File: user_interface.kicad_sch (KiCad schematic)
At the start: 33 parts, among them CN5 Line out, CN6 Headphone, J2 SWD, J3 I2C, J6 SPI, J9 Serial, P1 GPIO, SW4 BTN1, SW5 BTN2

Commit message: Start routing through the new signal layer.
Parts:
- removed R32: Zero, Resistor_SMD:R_2010_5025Metric, symbol Device:R_Small
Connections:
- net HPJ_R is gone; now on net HEADPHONE_R: CN6.3
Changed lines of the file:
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@@
 	(wire
 		(pts
-			(xy 212.09 53.34) (xy 220.98 53.34)
+			(xy 212.09 53.34) (xy 232.41 53.34)
 		)
 		(stroke
@@
 	(wire
 		(pts
-			(xy 226.06 53.34) (xy 232.41 53.34)
-		)
-		(stroke
-			(width 0)
-			(type default)
-		)
-	)
-	(wire
-		(pts
 			(xy 68.58 175.26) (xy 74.93 175.26)
 		)
@@
 		)
 	)
-	(label "HPJ_R"
-		(at 226.06 53.34 0)
-		(fields_autoplaced yes)
-		(effects
-			(font
-				(size 1.27 1.27)
-			)
-			(justify left bottom)
-		)
-	)
 	(label "BTN2_CR"
 		(at 171.45 48.26 0)
@@
 					(unit 1)
 				)
-			)
-		)
-	)
-	(symbol
-		(lib_id "Device:R_Small")
-		(at 223.52 53.34 90)
-		(unit 1)
-		(exclude_from_sim no)
-		(in_bom yes)
-		(on_board yes)
-		(dnp no)
-		(property "Reference" "R32"
-			(at 223.52 47.244 90)
-			(effects
-				(font
-					(size 1.27 1.27)
-				)
-			)
-		)
-		(property "Value" "Zero"
-			(at 223.52 49.276 90)
-			(effects
-				(font
-					(size 1.27 1.27)
-				)
-			)
-		)
-		(property "Footprint" "Resistor_SMD:R_2010_5025Metric"
-			(at 223.52 53.34 0)
-			(effects
-				(font
-					(size 1.27 1.27)
-				)
-				(hide yes)
-			)
-		)
-		(property "Datasheet" "~"
-			(at 223.52 53.34 0)
-			(effects
-				(font
-					(size 1.27 1.27)
-				)
-				(hide yes)
-			)
-		)
-		(property "Description" "Resistor, small symbol"
-			(at 223.52 53.34 0)
-			(effects
-				(font
-					(size 1.27 1.27)
-				)
-				(hide yes)
-			)
-		)
-		(property "LCSC" ""
-			(at 223.52 53.34 0)
-			(effects
-				(font
-					(size 1.27 1.27)
-				)
-				(hide yes)
-			)
-		)
-		(property "DPFNOTES" "For Routing"
-			(at 223.52 53.34 0)
-			(effects
-				(font
-					(size 1.27 1.27)
-				)
-				(hide yes)
-			)
-		)
-		(property "DPFURL" ""
-			(at 223.52 53.34 0)
-			(effects
-				(font
-					(size 1.27 1.27)
-				)
-				(hide yes)
-			)
-		)
-		(pin "1"
-		)
-		(pin "2"
-		)
-		(instances
-			(project "stm-midi-poc1"
-				(path "/7cd74113-1f92-4dcc-8610-19aa9fc81e5f/96c396b4-5394-4a50-9288-ad4476d1492f"
-					(reference "R32")
-					(unit 1)
-				)

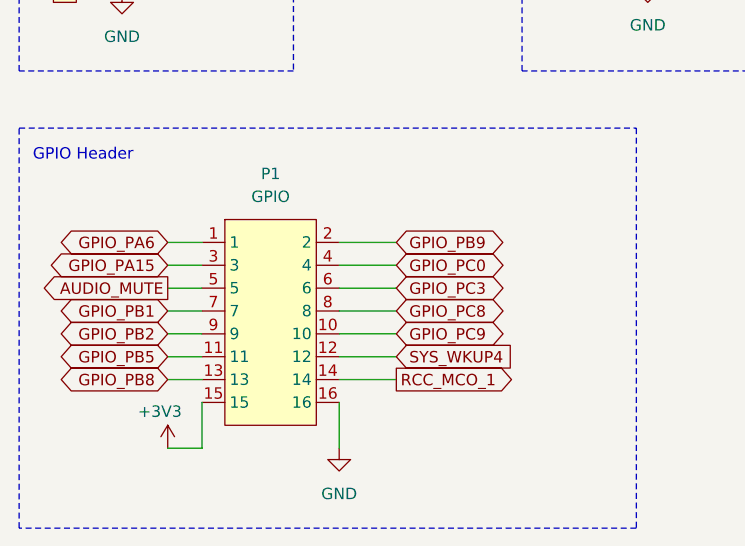
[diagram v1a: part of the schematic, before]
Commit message: All signals now routed through revised GPIO pinout. TODO: Put ground vias everywhere needed for signal vias.
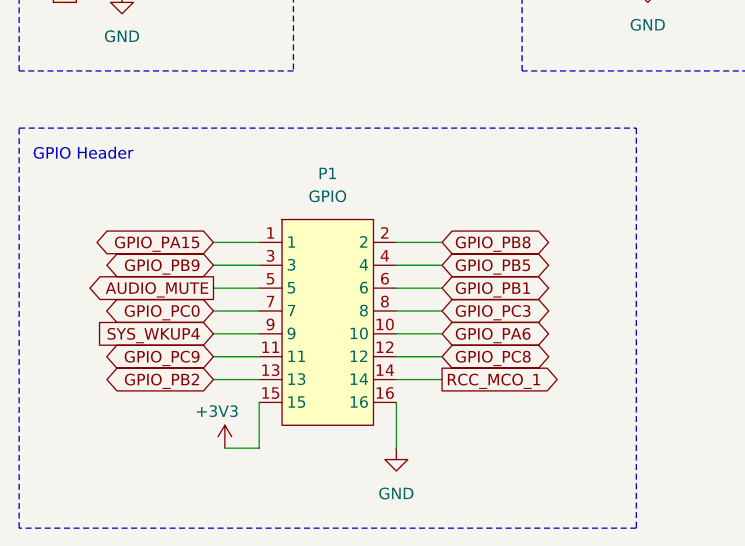
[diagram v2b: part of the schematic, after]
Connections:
- net GPIO_PA15: now also P1.1; no longer P1.3
- net GPIO_PA6: now also P1.10; no longer P1.1
- net GPIO_PB1: now also P1.6; no longer P1.7
- net GPIO_PB2: now also P1.13; no longer P1.9
- net GPIO_PB5: now also P1.4; no longer P1.11
- net GPIO_PB8: now also P1.2; no longer P1.13
- net GPIO_PB9: now also P1.3; no longer P1.2
- net GPIO_PC0: now also P1.7; no longer P1.4
- net GPIO_PC3: now also P1.8; no longer P1.6
- net GPIO_PC8: now also P1.12; no longer P1.8
- net GPIO_PC9: now also P1.11; no longer P1.10
- net SYS_WKUP4: now also P1.9; no longer P1.12
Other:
- moved on the sheet: P1

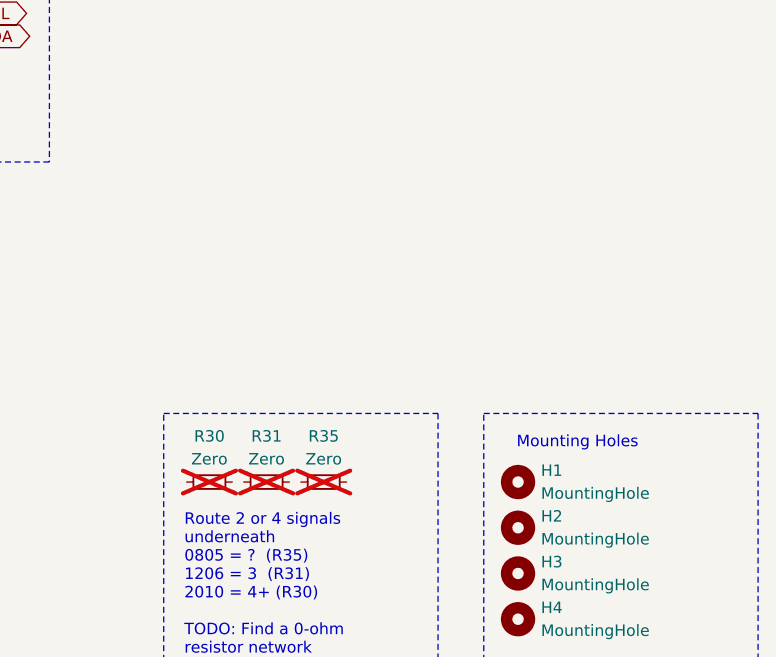
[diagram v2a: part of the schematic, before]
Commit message: 1. Update README with info on my KiCAD component library. 2. Add Fiducial markers. 3. Add LCSC IDs for all parts in BOM.
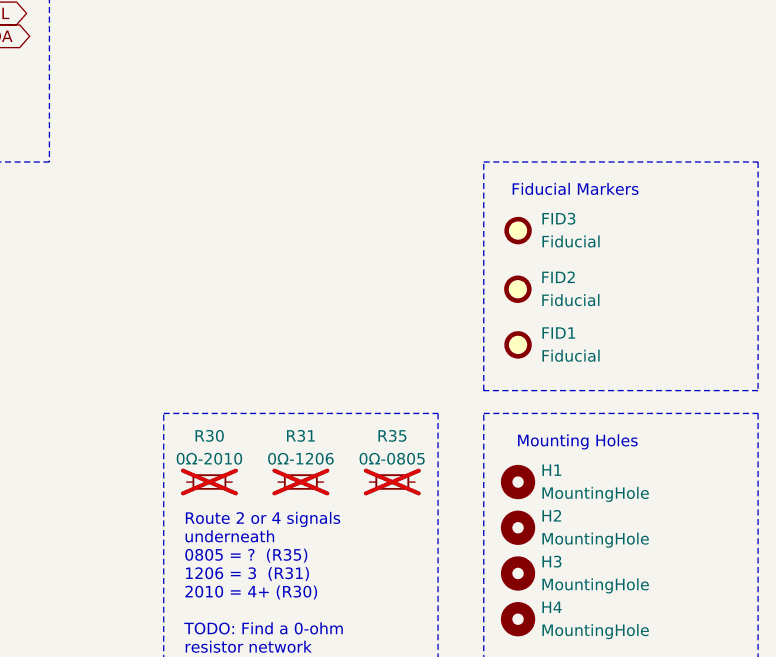
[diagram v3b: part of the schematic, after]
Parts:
- added FID1, FID2, FID3: Fiducial, Fiducial:Fiducial_1mm_Mask2mm, symbol Mechanical:Fiducial
- D4: DPFNOTES (none) -> THIS IS A RED ONE - FIND THE REAL ONE; LCSC (none) -> C2286
- D5: DPFNOTES (none) -> THIS IS A RED ONE; LCSC (none) -> C2286
- J2: DPFNOTES (none) -> Direct Insert 5P 2.54mm Single Row 1x5P Plugin,P=2.54mm Pin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; LCSC (none) -> C7430361
- J3: DPFNOTES (none) -> 8P 2.54mm Double Row 2x4P Plugin,P=2.54mm Pin Headers ROHS; LCSC (none) -> C5156676
- J6: LCSC (none) -> C7430361
- J9: LCSC (none) -> C5116483
- R10, R12: DPFNOTES (none) -> 100mW Thick Film Resistors 75V ±1% ±200ppm/℃ 100Ω 0603 Chip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; LCSC (none) -> C22775
- R11, R9: DPFNOTES (none) -> 100mW Thick Film Resistors 75V ±100ppm/℃ ±1% 4.7kΩ 0603 Chi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; LCSC (none) -> C23162
- R17, R18, R19, R20: DPFNOTES (none) -> 62.5mW Thick Film Resistors 50V ±100ppm/℃ ±1% 1.8kΩ 0402 Ch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; LCSC (none) -> C25871
- R30: value Zero -> 0Ω-2010; LCSC (none) -> C144433
- R31: value Zero -> 0Ω-1206; LCSC (none) -> C17888
- R35: value Zero -> 0Ω-0805; LCSC (none) -> C17477
- SW4, SW5: LCSC (none) -> C318884
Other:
- note added: "Fiducial Markers"
- moved on the sheet: R31, R35

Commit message: 1. Remove unused components on schematic. 2. Find other color LEDs in JLCPCB.
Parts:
- D4: DPFNOTES THIS IS A RED ONE - FIND THE REAL ONE -> 20mA 199mcd Colorless transparent lens -40℃~+85℃ 520nm~535n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; LCSC C2286 -> C72043
- D5: DPFNOTES THIS IS A RED ONE -> 5mA Colorless transparent lens -40℃~+85℃ 465nm~475nm Blue 1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; LCSC C2286 -> C72041
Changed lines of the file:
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@@
 	(title_block
 		(title "User Interface")
-		(date "2024-10-12")
+		(date "2024-10-26")
 		(rev "1")
 		(company "Douglas P. Fields, Jr.")
@@
 			)
 		)
-		(property "LCSC" "C2286"
+		(property "LCSC" "C72041"
 			(at 81.28 38.1 0)
 			(effects
@@
 			)
 		)
-		(property "DPFNOTES" "THIS IS A RED ONE"
+		(property "DPFNOTES" "5mA Colorless transparent lens -40℃~+85℃ 465nm~475nm Blue 120° 110mW 0603 LED Indication - Discrete ROHS (Note: If out of stock, Yellow is C72038)"
 			(at 81.28 38.1 0)
 			(effects
@@
 			)
 		)
-		(property "Datasheet" "~"
+		(property "Datasheet" "https://www.lcsc.com/datasheet/lcsc_datasheet_1810231112_Hubei-KENTO-Elec-KT-0603R_C2286.pdf"
 			(at 43.18 38.1 0)
 			(effects
@@
 			)
 		)
-		(property "Datasheet" "~"
+		(property "Datasheet" "https://www.lcsc.com/datasheet/lcsc_datasheet_1811101510_Everlight-Elec-19-217-GHC-YR1S2-3T_C72043.pdf"
 			(at 62.23 38.1 0)
 			(effects
@@
 			)
 		)
-		(property "LCSC" "C2286"
+		(property "LCSC" "C72043"
 			(at 62.23 38.1 0)
 			(effects
@@
 			)
 		)
-		(property "DPFNOTES" "THIS IS A RED ONE - FIND THE REAL ONE"
+		(property "DPFNOTES" "20mA 199mcd Colorless transparent lens -40℃~+85℃ 520nm~535nm Emerald 120° 110mW 3.3V 0603 LED Indication - Discrete ROHS"
 			(at 62.23 38.1 0)
 			(effects

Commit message: Found an in-stock blue LED but it is expensive.
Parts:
- D5: Basic Part (none) -> C72041 but not in stock ... 5mA Colorless transparent lens 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; DPFNOTES 5mA Colorless transparent lens -40℃~+85℃ 465nm~475nm Blue 1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 -> 20mA 145mcd Colorless transparent lens 470nm Blue 140° 3.2V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; DPFURL (none) -> https://wmsc.lcsc.com/wmsc/upload/file/pdf/v2/lcsc/23060611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; LCSC C72041 -> C5197644
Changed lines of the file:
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@@
 			)
 		)
-		(property "LCSC" "C72041"
+		(property "LCSC" "C5197644"
 			(at 81.28 38.1 0)
 			(effects
@@
 			)
 		)
-		(property "DPFNOTES" "5mA Colorless transparent lens -40℃~+85℃ 465nm~475nm Blue 120° 110mW 0603 LED Indication - Discrete ROHS (Note: If out of stock, Yellow is C72038)"
+		(property "DPFNOTES" "20mA 145mcd Colorless transparent lens 470nm Blue 140° 3.2V 0603 Light Emitting Diodes (LED) ROHS"
 			(at 81.28 38.1 0)
 			(effects
@@
 			)
 		)
-		(property "DPFURL" ""
+		(property "DPFURL" "https://wmsc.lcsc.com/wmsc/upload/file/pdf/v2/lcsc/2306061153_Wurth-Elektronik-150060BS75000_C5197644.pdf"
 			(at 81.28 38.1 0)
 			(effects
 				(font
+					(size 1.27 1.27)
+				)
+				(hide yes)
+			)
+		)
+		(property "Basic Part" "C72041 but not in stock ... 5mA Colorless transparent lens -40℃~+85℃ 465nm~475nm Blue 120° 110mW 0603 LED Indication - Discrete ROHS (Note: If out of stock, Yellow is C72038)"
+			(at 81.28 38.1 90)
+			(effects
+				(font

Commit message: Trying to get things ready for sending to JLCPCB
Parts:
- D5: DPFNOTES 20mA 145mcd Colorless transparent lens 470nm Blue 140° 3.2V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 -> This is YELLOW because the BLUE one is NOT in stock: 20mA C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; DPFURL https://wmsc.lcsc.com/wmsc/upload/file/pdf/v2/lcsc/23060611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 -> https://www.lcsc.com/datasheet/lcsc_datasheet_1810101813_Ev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; LCSC C5197644 -> C72038
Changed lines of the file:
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@@
 			)
 		)
-		(property "LCSC" "C5197644"
+		(property "LCSC" "C72038"
 			(at 81.28 38.1 0)
 			(effects
@@
 			)
 		)
-		(property "DPFNOTES" "20mA 145mcd Colorless transparent lens 470nm Blue 140° 3.2V 0603 Light Emitting Diodes (LED) ROHS"
+		(property "DPFNOTES" "This is YELLOW because the BLUE one is NOT in stock: 20mA Colorless transparent lens -40℃~+85℃ 585.5nm~591.5nm Yellow 120° 60mW 0603 LED Indication - Discrete ROHS"
 			(at 81.28 38.1 0)
 			(effects
@@
 			)
 		)
-		(property "DPFURL" "https://wmsc.lcsc.com/wmsc/upload/file/pdf/v2/lcsc/2306061153_Wurth-Elektronik-150060BS75000_C5197644.pdf"
+		(property "DPFURL" "https://www.lcsc.com/datasheet/lcsc_datasheet_1810101813_Everlight-Elec-19-213-Y2C-CQ2R2L-3T-CY_C72038.pdf"
 			(at 81.28 38.1 0)
 			(effects

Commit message: Reviewing every item in the BOM against LCSC database. Found several errors already. Part way done.
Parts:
- C18, C19: DPFNOTES (none) -> 50V 100nF X7R ±10% 0402 Multilayer Ceramic Capacitors MLCC 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; JLC Basic Part (none) -> Basic
- CN5, CN6: DPFNOTES In-stock 3.5mm TRS -> -20℃~+70℃ 3.5mm Headphone Jack 30V 500mA SMD Audio Connecto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; JLC Basic Part (none) -> Extended; Manu Part (none) -> PJ-321A-4A; Manufacturer (none) -> Korean Hroparts Elec
- D3: DPFNOTES Hubei KENTO Elec KT-0603R -> -40℃~+85℃ Red 0603 LED Indication - Discrete ROHS; JLC Basic Part (none) -> Basic
- D4: JLC Basic Part (none) -> Extended; Manu Part (none) -> 19-217/GHC-YR1S2/3T
- D5: Basic Part C72041 but not in stock ... 5mA Colorless transparent lens 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 -> (none); JLC Basic Part (none) -> Basic - C72041 but not in stock ... 5mA Colorless transpare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; Manu Part (none) -> 19-213/Y2C-CQ2R2L/3T(CY)
- J2: JLC Basic Part (none) -> Extended; Manu Part (none) -> DS1021-1x5SF11-B; Manufacturer (none) -> CONNFLY Elec
- J3: JLC Basic Part (none) -> Extended; Manu Part (none) -> PZ2.54-2*4; Manufacturer (none) -> ZHOURI
- J6: DPFNOTES (none) -> Direct Insert 5P 2.54mm Single Row 1x5P Plugin,P=2.54mm Pin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; JLC Basic Part (none) -> Extended; Manu Part (none) -> DS1021-1x5SF11-B; Manufacturer (none) -> CONNFLY Elec
- J9: DPFNOTES (none) -> 4P 2.54mm Single Row 1x4P Plugin,P=2.54mm Pin Headers ROHS; JLC Basic Part (none) -> Extended; Manu Part (none) -> 2.54-1*4; Manufacturer (none) -> ZHOURI
- P1: JLC Basic Part (none) -> Extended; Manu Part (none) -> 2.54-2*8P; Manufacturer (none) -> BOOMELE(Boom Precision Elec)
- R10, R12: DPFNOTES 100mW Thick Film Resistors 75V ±1% ±200ppm/℃ 100Ω 0603 Chip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 -> 62.5mW Thick Film Resistors 50V ±1% ±200ppm/℃ 100Ω 0402 Chi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; FIXME (none) -> WRONG; JLC Basic Part (none) -> Basic; LCSC C22775 -> C25076; Manu Part (none) -> 0402WGF1000TCE; Manufacturer (none) -> UNI-ROYAL(Uniroyal Elec)
- R11, R9: DPFNOTES 100mW Thick Film Resistors 75V ±100ppm/℃ ±1% 4.7kΩ 0603 Chi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 -> 62.5mW Thick Film Resistors 50V ±100ppm/℃ ±1% 4.7kΩ 0402 Ch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; JLC Basic Part (none) -> Basic; LCSC C23162 -> C25900; Manu Part (none) -> 0402WGF4701TCE; Manufacturer (none) -> UNI-ROYAL(Uniroyal Elec)
- R6, R7, R8: DPFNOTES (none) -> 62.5mW Thick Film Resistors 50V ±100ppm/℃ ±1% 1.5kΩ 0402 Ch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; JLC Basic Part (none) -> Basic; Manu Part (none) -> 0402WGF1501TCE; Manufacturer (none) -> UNI-ROYAL(Uniroyal Elec)

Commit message: Finished checking all parts against LCSC IDs. Found remaining errors. Added manufacturer part numbers to all parts.
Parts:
- C18, C19: Manu Part (none) -> CL05B104KB54PNC; Manufacturer (none) -> Samsung Electro-Mechanics
- D3: Manu Part (none) -> KT-0603R; Manufacturer (none) -> Hubei KENTO Elec
- D4, D5: Manufacturer (none) -> Everlight Elec
- R10, R12: FIXME WRONG -> (none)
- R17, R18, R19, R20: JLC Basic Part (none) -> Extended - Basic is C4177 but is 0603; Manu Part (none) -> 0402WGF1801TCE; Manufacturer (none) -> UNI-ROYAL(Uniroyal Elec)
- R30: JLC Basic Part (none) -> Extended; Manu Part (none) -> AC2010JK-070RL; Manufacturer (none) -> YAGEO
- R31: JLC Basic Part (none) -> Basic; Manu Part (none) -> 1206W4F0000T5E; Manufacturer (none) -> UNI-ROYAL(Uniroyal Elec)
- R35: JLC Basic Part (none) -> Basic; Manu Part (none) -> 0805W8F0000T5E; Manufacturer (none) -> UNI-ROYAL(Uniroyal Elec)
- SW4, SW5: DPFNOTES (none) -> None Without 50mA 5.1mm 100000 Times 160gf 12V 5.1mm 1.5mm 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; JLC Basic Part (none) -> Basic; Manu Part (none) -> TS-1187A-B-A-B; Manufacturer (none) -> XKB Connection
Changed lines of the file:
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@@
 			)
 		)
-		(property "Datasheet" "~"
+		(property "Datasheet" "https://www.lcsc.com/datasheet/lcsc_datasheet_2206010216_UNI-ROYAL-Uniroyal-Elec-0805W8F0000T5E_C17477.pdf"
 			(at 220.98 142.24 0)
 			(effects
@@
 			)
 		)
-		(property "Manu Part" ""
+		(property "Manu Part" "0805W8F0000T5E"
 			(at 220.98 142.24 0)
 			(effects
@@
 			)
 		)
-		(property "Manufacturer" ""
+		(property "Manufacturer" "UNI-ROYAL(Uniroyal Elec)"
 			(at 220.98 142.24 0)
 			(effects
@@
 			)
 		)
+		(property "JLC Basic Part" "Basic"
+			(at 220.98 142.24 0)
+			(effects
+				(font
+					(size 1.27 1.27)
+				)
+				(hide yes)
+			)
+		)
 		(pin "1"
 		)
@@
 			)
 		)
-		(property "Manufacturer" ""
+		(property "Manufacturer" "Everlight Elec"
 			(at 81.28 38.1 0)
 			(effects
@@
 			)
 		)
-		(property "DPFNOTES" ""
+		(property "DPFNOTES" "None Without 50mA 5.1mm 100000 Times 160gf 12V 5.1mm 1.5mm Round Button Standing paste SPST SMD Tactile Switches ROHS"
 			(at 123.19 45.72 0)
 			(effects
@@
 			)
 		)
-		(property "Manu Part" ""
+		(property "Manu Part" "TS-1187A-B-A-B"
 			(at 123.19 45.72 0)
 			(effects
@@
 			)
 		)
-		(property "Manufacturer" ""
+		(property "Manufacturer" "XKB Connection"
 			(at 123.19 45.72 0)
 			(effects
@@
 			)
 		)
+		(property "JLC Basic Part" "Basic"
+			(at 123.19 45.72 0)
+			(effects
+				(font
+					(size 1.27 1.27)
+				)
+				(hide yes)
+			)
+		)
 		(pin "1"
 		)
@@
 			)
 		)
-		(property "Manu Part" ""
+		(property "Manu Part" "TS-1187A-B-A-B"
 			(at 161.29 45.72 0)
 			(effects
@@
 			)
 		)
-		(property "Manufacturer" ""
+		(property "Manufacturer" "XKB Connection"
 			(at 161.29 45.72 0)
 			(effects
@@
 			)
 		)
+		(property "DPFNOTES" "None Without 50mA 5.1mm 100000 Times 160gf 12V 5.1mm 1.5mm Round Button Standing paste SPST SMD Tactile Switches ROHS"
+			(at 161.29 45.72 0)
+			(effects
+				(font
+					(size 1.27 1.27)
+				)
+				(hide yes)
+			)
+		)
+		(property "JLC Basic Part" "Basic"
+			(at 161.29 45.72 0)
+			(effects
+				(font
+					(size 1.27 1.27)
+				)
+				(hide yes)
+			)
+		)
 		(pin "1"
 		)
@@
 			)
 		)
-		(property "FIXME" "WRONG"
+		(property "FIXME" ""
 			(at 133.35 52.07 0)
 			(effects
@@
 			)
 		)
-		(property "Manu Part" ""
+		(property "Manu Part" "0402WGF1801TCE"
 			(at 109.22 83.82 0)
 			(effects
@@
 			)
 		)
-		(property "Manufacturer" ""
+		(property "Manufacturer" "UNI-ROYAL(Uniroyal Elec)"
 			(at 109.22 83.82 0)
 			(effects
@@
 			)
 		)
+		(property "JLC Basic Part" "Extended - Basic is C4177 but is 0603"
+			(at 109.22 83.82 0)
+			(effects
+				(font
+					(size 1.27 1.27)
+				)
+				(hide yes)
+			)
+		)
 		(pin "1"
 		)
@@
 			)
 		)
-		(property "FIXME" "WRONG"
+		(property "FIXME" ""
 			(at 171.45 52.07 0)
 			(effects
@@
 			)
 		)
-		(property "Manu Part" ""
+		(property "Manu Part" "KT-0603R"
 			(at 43.18 38.1 0)
 			(effects
@@
 			)
 		)
-		(property "Manufacturer" ""
+		(property "Manufacturer" "Hubei KENTO Elec"
 			(at 43.18 38.1 0)
 			(effects
@@
 			)
 		)
-		(property "Manufacturer" ""
+		(property "Manufacturer" "Everlight Elec"
 			(at 62.23 38.1 0)
 			(effects
@@
 			)
 		)
-		(property "Manu Part" ""
+		(property "Manu Part" "0402WGF1801TCE"
 			(at 152.4 83.82 0)
 			(effects
@@
 			)
 		)
-		(property "Manufacturer" ""
+		(property "Manufacturer" "UNI-ROYAL(Uniroyal Elec)"
 			(at 152.4 83.82 0)
 			(effects
@@
 			)
 		)
+		(property "JLC Basic Part" "Extended - Basic is C4177 but is 0603"
+			(at 152.4 83.82 0)
+			(effects
+				(font
+					(size 1.27 1.27)
+				)
+				(hide yes)
+			)
+		)
 		(pin "1"
 		)
@@
 			)
 		)
-		(property "Manu Part" ""
+		(property "Manu Part" "CL05B104KB54PNC"
 			(at 171.45 44.45 0)
 			(effects
@@
 			)
 		)
-		(property "Manufacturer" ""
+		(property "Manufacturer" "Samsung Electro-Mechanics"
 			(at 171.45 44.45 0)
 			(effects
@@
 			)
 		)
-		(property "Datasheet" "~"
+		(property "Datasheet" "https://www.lcsc.com/datasheet/lcsc_datasheet_2206010200_UNI-ROYAL-Uniroyal-Elec-1206W4F0000T5E_C17888.pdf"
 			(at 210.82 142.24 0)
 			(effects
@@
 			)
 		)
-		(property "Manu Part" ""
+		(property "Manu Part" "1206W4F0000T5E"
 			(at 210.82 142.24 0)
 			(effects
@@
 			)
 		)
-		(property "Manufacturer" ""
+		(property "Manufacturer" "UNI-ROYAL(Uniroyal Elec)"
 			(at 210.82 142.24 0)
 			(effects
@@
 			)
 		)
+		(property "JLC Basic Part" "Basic"
+			(at 210.82 142.24 0)
+			(effects
+				(font
+					(size 1.27 1.27)
+				)
+				(hide yes)
+			)
+		)
 		(pin "1"
 		)
@@
 			)
 		)
-		(property "Manu Part" ""
+		(property "Manu Part" "0402WGF1801TCE"
 			(at 119.38 83.82 0)
 			(effects
@@
 			)
 		)
-		(property "Manufacturer" ""
+		(property "Manufacturer" "UNI-ROYAL(Uniroyal Elec)"
 			(at 119.38 83.82 0)
 			(effects
@@
 			)
 		)
+		(property "JLC Basic Part" "Extended - Basic is C4177 but is 0603"
+			(at 119.38 83.82 0)
+			(effects
+				(font
+					(size 1.27 1.27)
+				)
+				(hide yes)
+			)
+		)
 		(pin "1"
 		)
@@
 			)
 		)
-		(property "Manu Part" ""
+		(property "Manu Part" "0402WGF1801TCE"
 			(at 162.56 83.82 0)
 			(effects
@@
 			)
 		)
-		(property "Manufacturer" ""
+		(property "Manufacturer" "UNI-ROYAL(Uniroyal Elec)"
 			(at 162.56 83.82 0)
 			(effects
@@
 			)
 		)
+		(property "JLC Basic Part" "Extended - Basic is C4177 but is 0603"
+			(at 162.56 83.82 0)
+			(effects
+				(font
+					(size 1.27 1.27)
+				)
+				(hide yes)
+			)
+		)
 		(pin "1"
 		)
@@
 			)
 		)
-		(property "Manu Part" ""
+		(property "Manu Part" "CL05B104KB54PNC"
 			(at 133.35 44.45 0)
 			(effects
@@
 			)
 		)
-		(property "Manufacturer" ""
+		(property "Manufacturer" "Samsung Electro-Mechanics"
 			(at 133.35 44.45 0)
 			(effects
@@
 			)
 		)
-		(property "Datasheet" "~"
+		(property "Datasheet" "https://www.lcsc.com/datasheet/lcsc_datasheet_2304140030_YAGEO-AC2010JK-070RL_C144433.pdf"
 			(at 200.66 142.24 0)
 			(effects
@@
 			)
 		)
-		(property "Manu Part" ""
+		(property "Manu Part" "AC2010JK-070RL"
 			(at 200.66 142.24 0)
 			(effects
@@
 			)
 		)
-		(property "Manufacturer" ""
+		(property "Manufacturer" "YAGEO"
 			(at 200.66 142.24 0)
 			(effects
@@
 			(at 200.66 142.24 0)
 			(effects
+				(font
+					(size 1.27 1.27)
+				)
+				(hide yes)
+			)
+		)
+		(property "JLC Basic Part" "Extended"
+			(at 200.66 142.24 0)
+			(effects
